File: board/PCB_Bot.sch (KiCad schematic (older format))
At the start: 16 parts, among them J1 Screw_Terminal_01x06, J2 Conn_02x15_Top_Bottom, J3 Conn_02x15_Top_Bottom, U1 TB6612FNG, U2 LSM9DS1

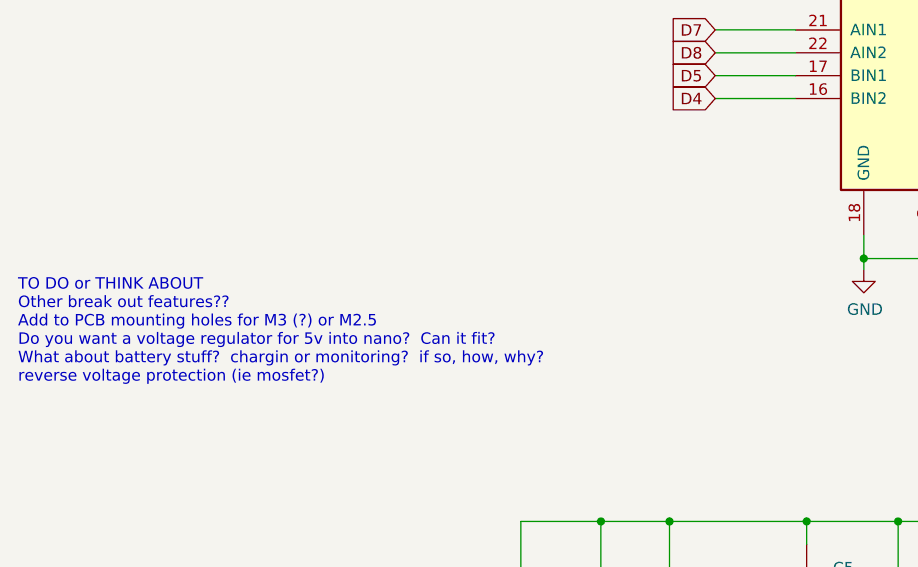
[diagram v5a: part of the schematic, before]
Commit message: update notes in schematic to better align w/ todo list
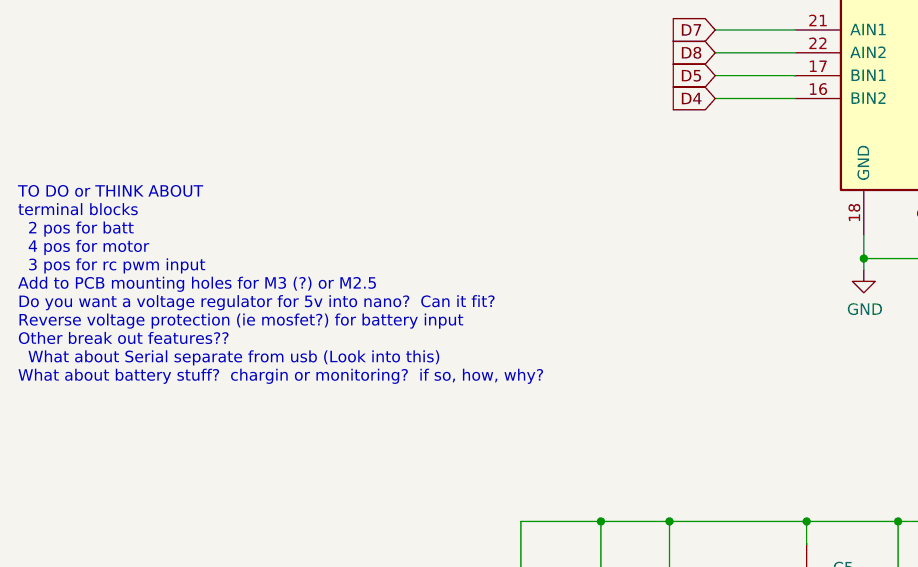
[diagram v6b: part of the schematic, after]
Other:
- note added: "TO DO or THINK ABOUT\nterminal blocks\n 2 pos for batt\n 4 pos for motor\n 3 pos for rc pwm input\nAdd to PCB mounting holes for M3 (?) or M2.5\nDo you want a voltage regulator for 5v into nano? Can it fit?\nReverse voltage protection (ie mosfet?) for battery input\nOther break out features??\n What about Serial separate from usb (Look into this)\nWhat about battery stuff? chargin or monitoring? 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"
- note removed: "TO DO or THINK ABOUT\nOther break out features??\nAdd to PCB mounting holes for M3 (?) or M2.5\nDo you want a voltage regulator for 5v into nano? Can it fit?\nWhat about battery stuff? chargin or monitoring? if so, how, why?\nreverse voltage protection (ie mosfet?)"
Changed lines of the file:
@@
 3V3
 Text Notes 650  3900 0    50   ~ 0
-TO DO or THINK ABOUT\nOther break out features??\nAdd to PCB mounting holes for M3 (?) or M2.5\nDo you want a voltage regulator for 5v into nano?  Can it fit?\nWhat about battery stuff?  chargin or monitoring?  if so, how, why?\nreverse voltage protection (ie mosfet?)
+TO DO or THINK ABOUT\nterminal blocks\n  2 pos for batt\n  4 pos for motor\n  3 pos for rc pwm input\nAdd to PCB mounting holes for M3 (?) or M2.5\nDo you want a voltage regulator for 5v into nano?  Can it fit?\nReverse voltage protection (ie mosfet?) for battery input\nOther break out features??\n  What about Serial separate from usb (Look into this)\nWhat about battery stuff?  chargin or monitoring?  if so, how, why?\n
 $Comp
 L power:+7.5V #PWR01
